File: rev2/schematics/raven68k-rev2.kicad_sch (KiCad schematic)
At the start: 16 parts, among them J1 CPLD_JTAG, SW1 RESET_SW, U1 MCP100-465D, U2 68010D, U3 XC9572XL-TQ100, X1 CLOCK

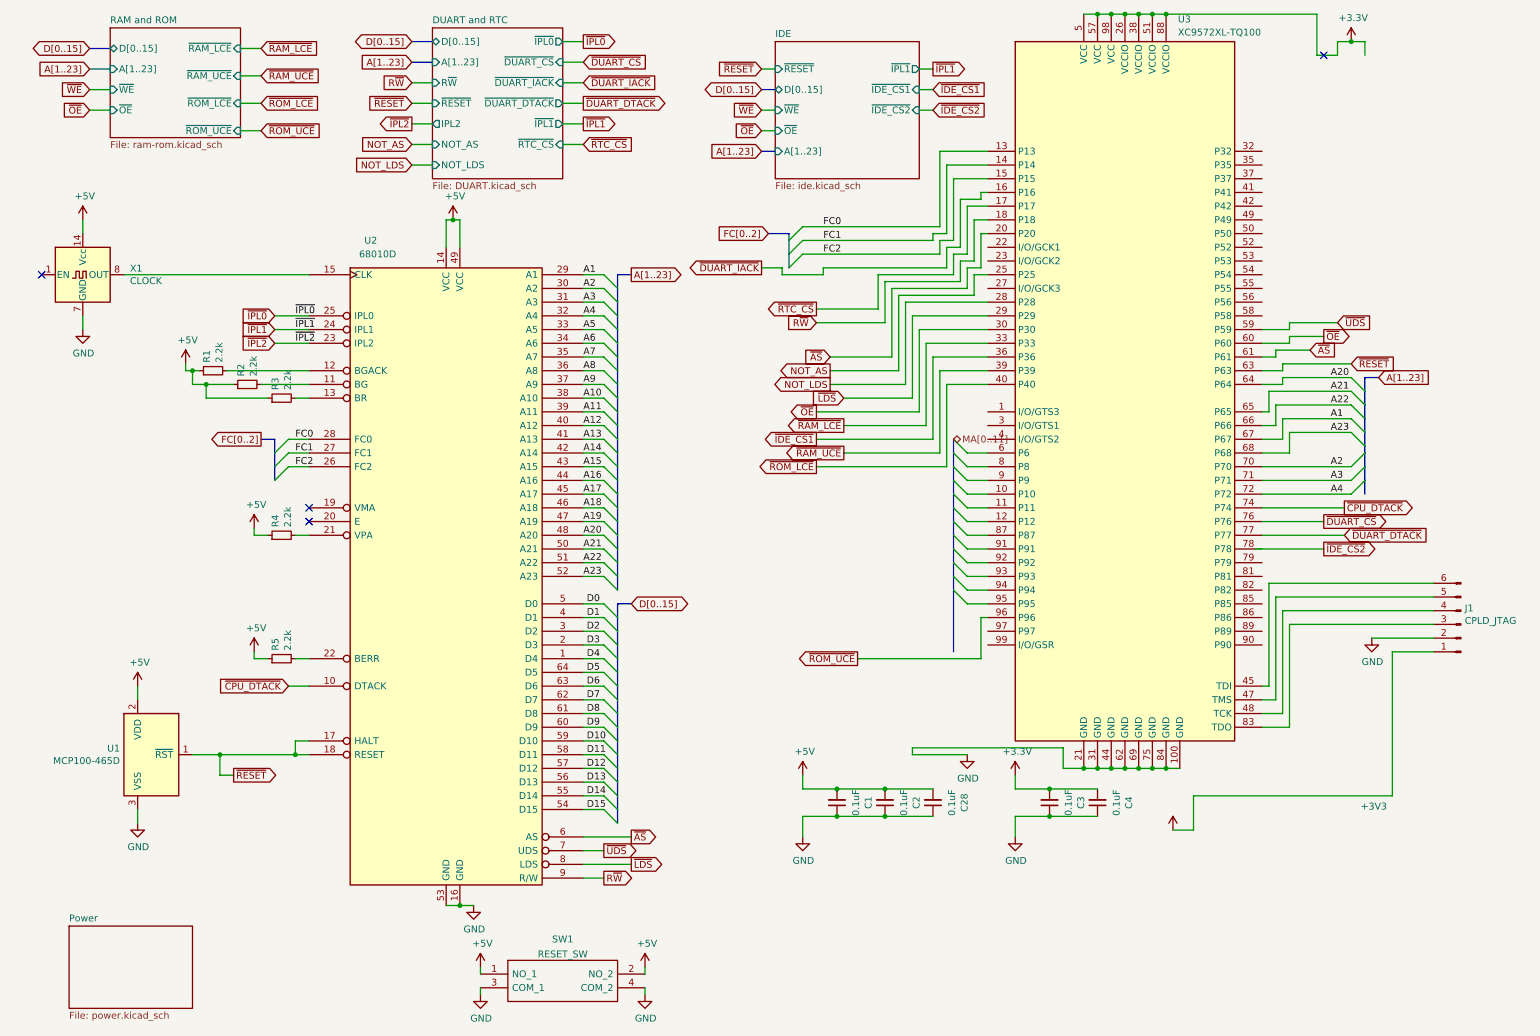
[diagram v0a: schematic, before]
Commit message: Fixed Bus connections. Added SIMM control connections to the CPLD. Added missing symbols from rev1 library. Cleaned up some SRAM related control signals that are no longer needed.
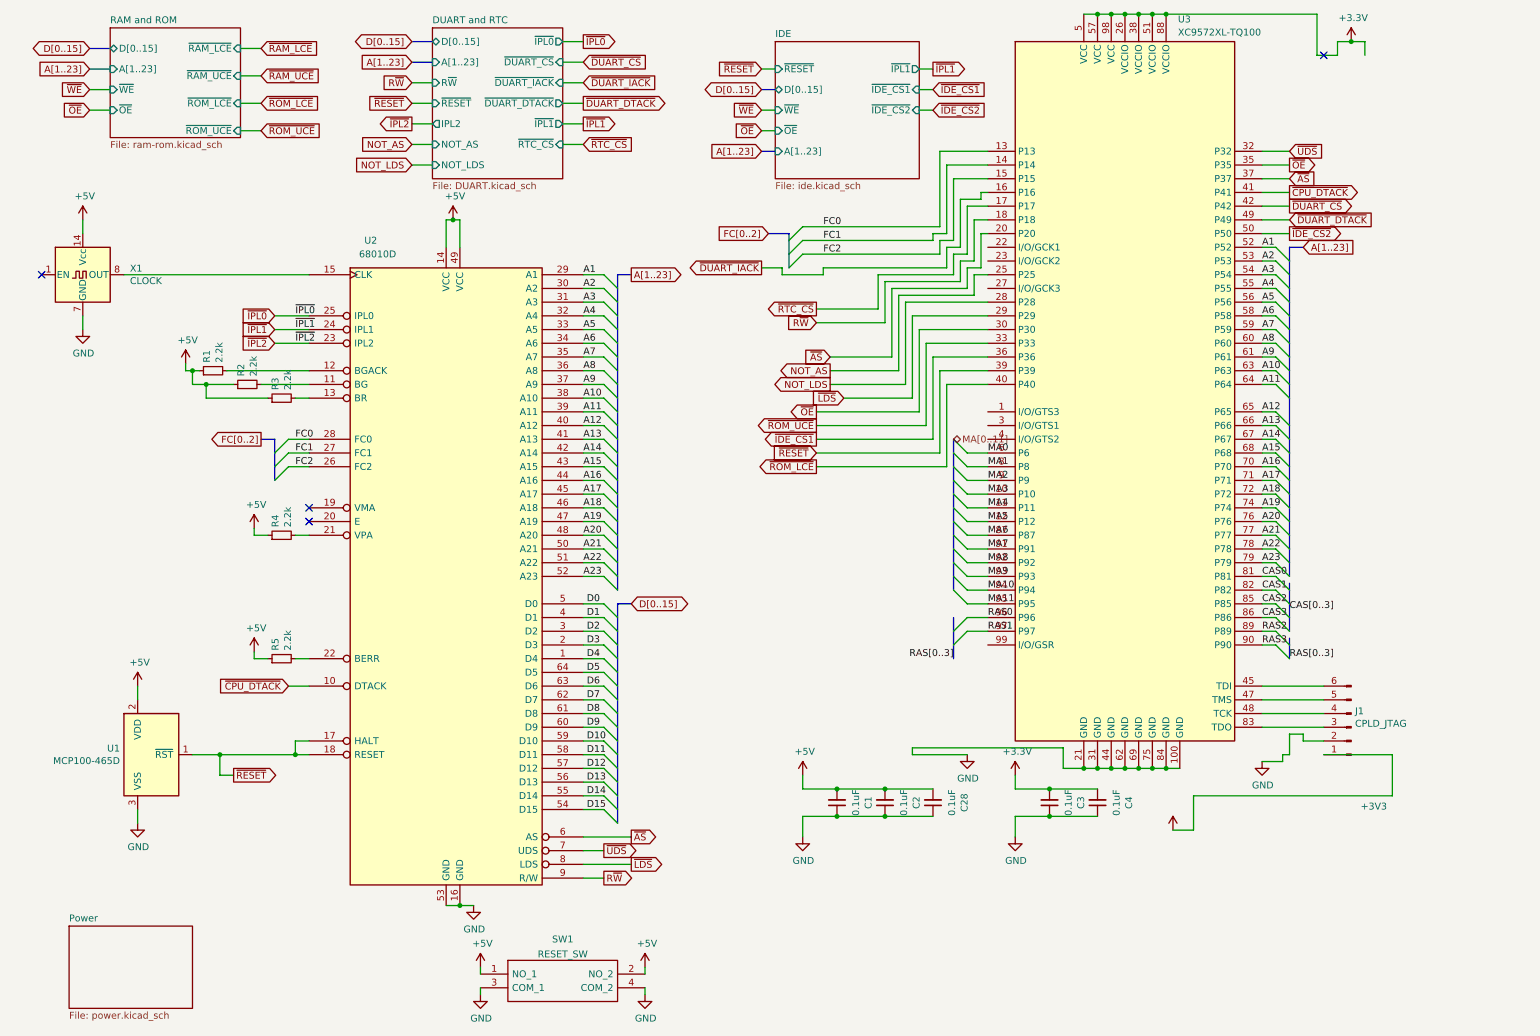
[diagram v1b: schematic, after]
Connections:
- net A1: now also U3.52 (P52); no longer U3.67 (P67)
- net A10: now also U3.63 (P63)
- net A11: now also U3.64 (P64)
- net A12: now also U3.65 (P65)
- net A13: now also U3.66 (P66)
- net A14: now also U3.67 (P67)
- net A15: now also U3.68 (P68)
- net A16: now also U3.70 (P70)
- net A17: now also U3.71 (P71)
- net A18: now also U3.72 (P72)
- net A19: now also U3.74 (P74)
- net A2: now also U3.53 (P53); no longer U3.70 (P70)
- net A20: now also U3.76 (P76); no longer U3.64 (P64)
- net A21: now also U3.77 (P77); no longer U3.65 (P65)
- net A22: now also U3.78 (P78); no longer U3.66 (P66)
- net A23: now also U3.79 (P79); no longer U3.68 (P68)
- net A3: now also U3.54 (P54); no longer U3.71 (P71)
- net A4: now also U3.55 (P55); no longer U3.72 (P72)
- net A5: now also U3.56 (P56)
- net A6: now also U3.58 (P58)
- net A7: now also U3.59 (P59)
- net A8: now also U3.60 (P60)
- net A9: now also U3.61 (P61)
- net ~{AS}: now also U3.37 (P37); no longer U3.61 (P61)
- net ~{CPU_DTACK}: now also U3.41 (P41); no longer U3.74 (P74)
- net ~{DUART_CS}: now also U3.42 (P42); no longer U3.76 (P76)
- net ~{DUART_DTACK}: now also U3.49 (P49); no longer U3.77 (P77)
- net ~{IDE_CS2}: now also U3.50 (P50)
- net ~{OE}: now also U3.35 (P35); no longer U3.60 (P60)
- net ~{RAM_LCE}: no longer U3.33 (P33)
- net ~{RAM_UCE}: no longer U3.39 (P39)
- net ~{RESET}: now also U3.39 (P39); no longer U3.63 (P63)
- net ~{ROM_UCE}: now also U3.33 (P33); no longer U3.96 (P96)
- net ~{UDS}: now also U3.32 (P32); no longer U3.59 (P59)
- net MA3: now reaches U3.10 (P10)
- net MA4: now reaches U3.11 (P11)
- net MA5: now reaches U3.12 (P12)
- net MA0: now reaches U3.6 (P6)
- net MA1: now reaches U3.8 (P8)
- net CAS0: now reaches U3.81 (P81)
- net CAS1: now reaches U3.82 (P82)
- net CAS2: now reaches U3.85 (P85)
- net CAS3: now reaches U3.86 (P86)
- net MA6: now reaches U3.87 (P87)
- net RAS2: now reaches U3.89 (P89)
- net MA2: now reaches U3.9 (P9)
- net RAS3: now reaches U3.90 (P90)
- net MA7: now reaches U3.91 (P91)
- net MA8: now reaches U3.92 (P92)
- net MA9: now reaches U3.93 (P93)
- net MA10: now reaches U3.94 (P94)
- net MA11: now reaches U3.95 (P95)
- net RAS1: now reaches U3.97 (P97)
- new net RAS0: U3.96 (P96)
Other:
- moved on the sheet: J1

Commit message: Added hierarchical labels from main sheet to RAM and ROM sheet.
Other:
- sheet RAM and ROM ports: added none; removed ~{RAM_LCE}, ~{RAM_UCE}
